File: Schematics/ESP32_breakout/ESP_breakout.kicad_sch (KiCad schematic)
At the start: 25 parts, among them U1 ESP32-S3-WROOM-1-N16R2, U2 TLV75801PDRV, U3 PD_D3V3XA4B10LP, U4 CAN_T_SN65HVD230DR

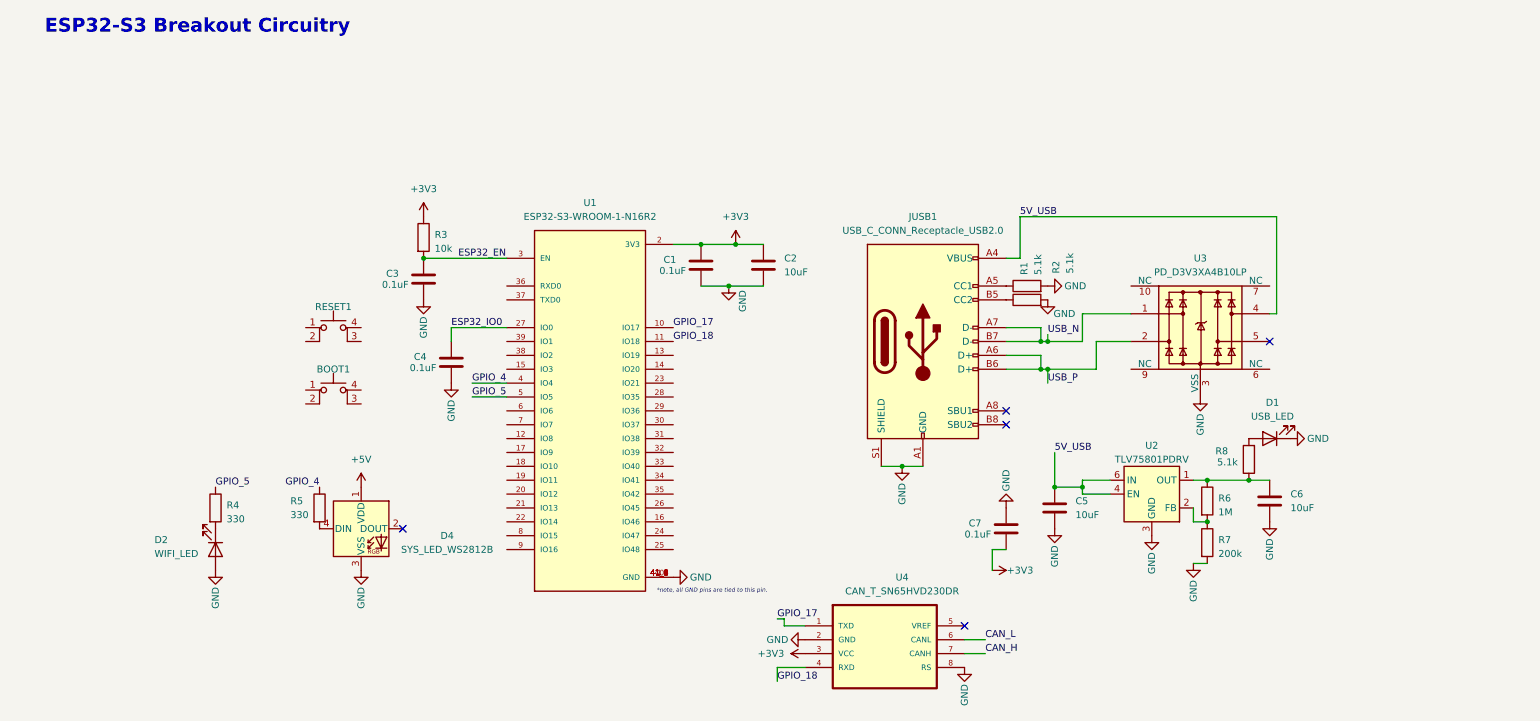
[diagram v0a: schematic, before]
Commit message: update breakout circuitry (check documentation on notion), power module.
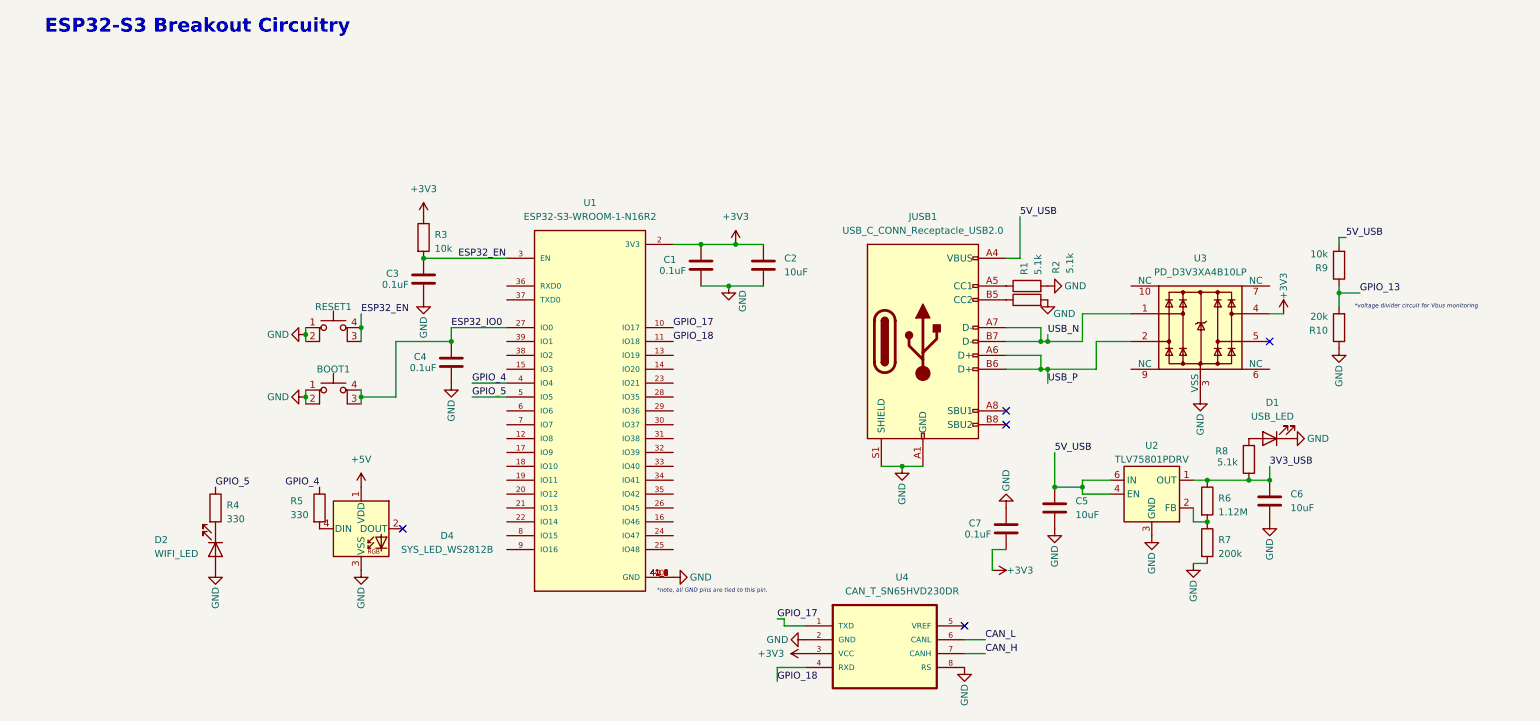
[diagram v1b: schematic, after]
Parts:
- added R10: 20k, Resistor_SMD:R_0603_1608Metric, symbol Device:R
- added R9: 10k, Resistor_SMD:R_0603_1608Metric, symbol Device:R
- R6: value 1M -> 1.12M
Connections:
- net +3V3: now also U3.4
- net 5V_USB: now also R9.2; no longer U3.4
- net ESP32_EN: now also RESET1.3 (K), RESET1.4 (A)
- net ESP32_IO0: now also BOOT1.3 (K), BOOT1.4 (A)
- net GND: now also BOOT1.1, BOOT1.2, RESET1.1, RESET1.2, R10.1
- net 3V3_USB: now reaches C6.1, R6.1, R8.1, U2.1 (OUT)
- new net GPIO_13: R10.2, R9.1
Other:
- note added: "*voltage divider circuit for Vbus monitoring"

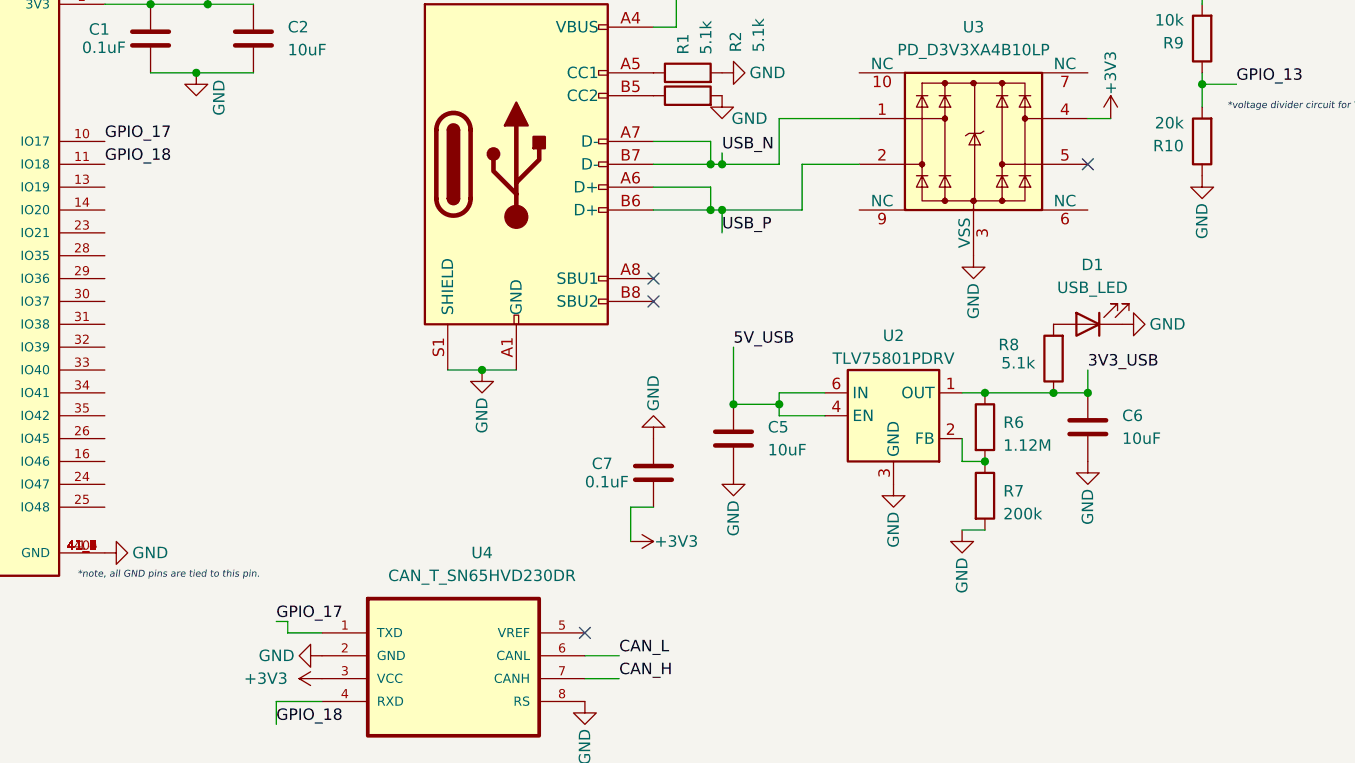
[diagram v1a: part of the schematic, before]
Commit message: add power module with ORing circuit, add datasheets on each symbol.
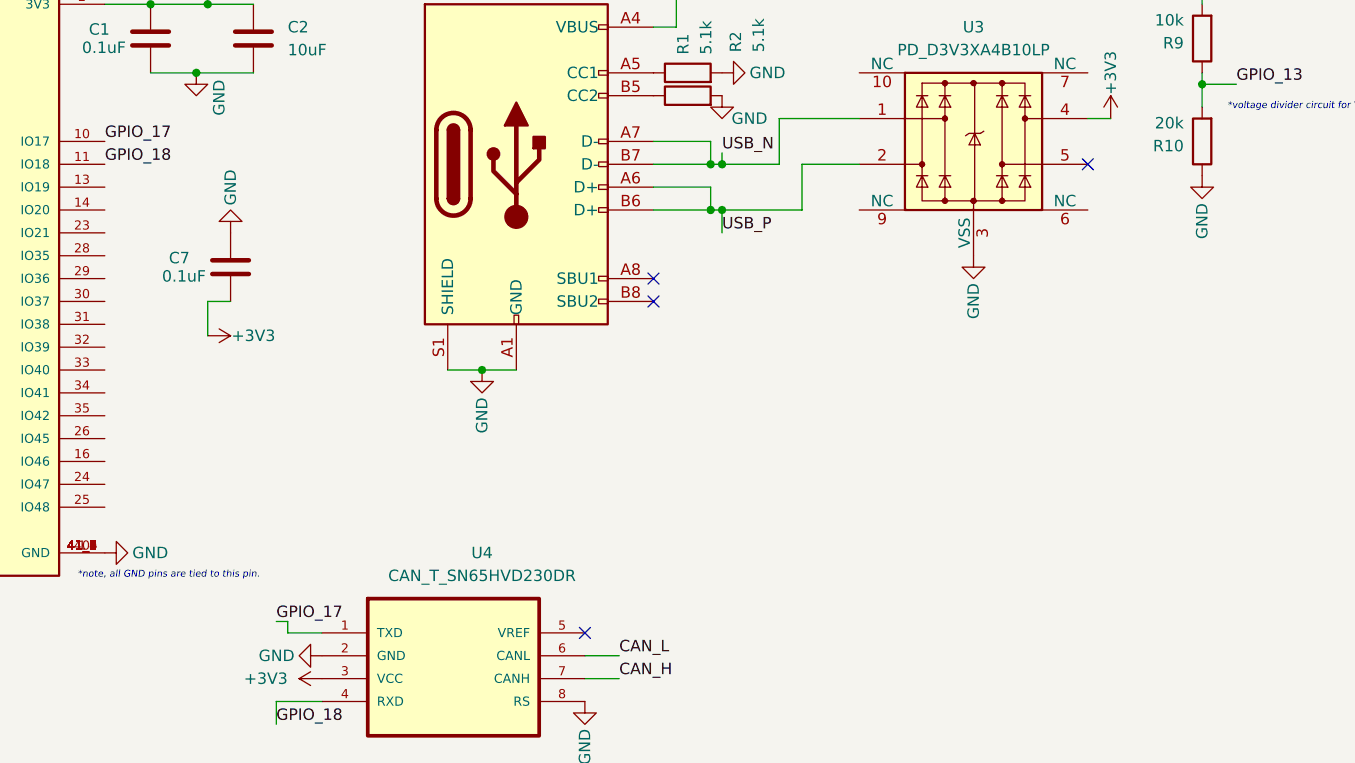
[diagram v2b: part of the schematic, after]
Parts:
- removed C5, C6: 10uF, Capacitor_SMD:C_0603_1608Metric, symbol Device:C
- removed D1: USB_LED, LED_SMD:LED_0603_1608Metric, symbol Device:LED
- removed R6: 1.12M, Resistor_SMD:R_0603_1608Metric, symbol Device:R
- removed R7: 200k, Resistor_SMD:R_0603_1608Metric, symbol Device:R
- removed R8: 5.1k, Resistor_SMD:R_0603_1608Metric, symbol Device:R
- removed U2: TLV75801PDRV, Package_SON:WSON-6-1EP_2x2mm_P0.65mm_EP1x1.6mm, symbol Regulator_Linear:TLV75801PDRV
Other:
- title: ESP32-S3 Module Breakout Circuitry -> ESP32-S3 Breakout Circuitry
- moved on the sheet: C7

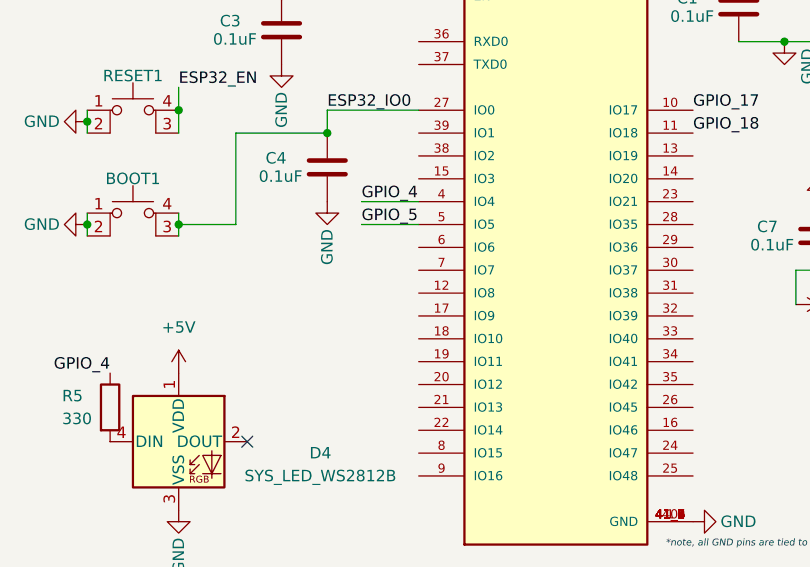
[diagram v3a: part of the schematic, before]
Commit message: finish sensor circuitry & add sensor documentation to notion.
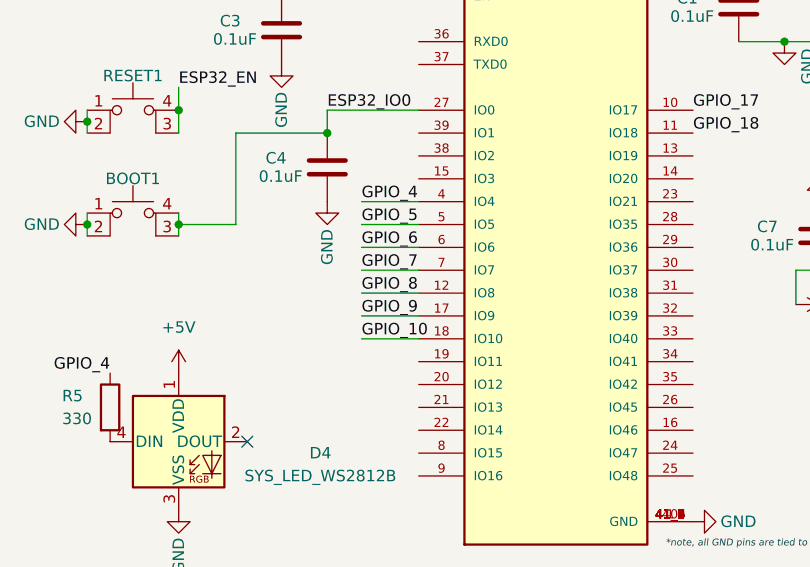
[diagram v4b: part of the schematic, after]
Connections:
- net GPIO_8: now reaches U1.12 (IO8)
- net GPIO_9: now reaches U1.17 (IO9)
- net GPIO_10: now reaches U1.18 (IO10)
- net GPIO_6: now reaches U1.6 (IO6)
- net GPIO_7: now reaches U1.7 (IO7)
